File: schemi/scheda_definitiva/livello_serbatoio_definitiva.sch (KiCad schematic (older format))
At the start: 43 parts, among them J1 USB_B, J2 BTN_LED_GROUP, J3 CONN_LCD, J4 CONN_US, J5 ICSP, J6 Exp_Analog_2, J7 Exp_Analog, SW1 SW_RST, U1 FT232RL, U2 ATmega328P-PU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

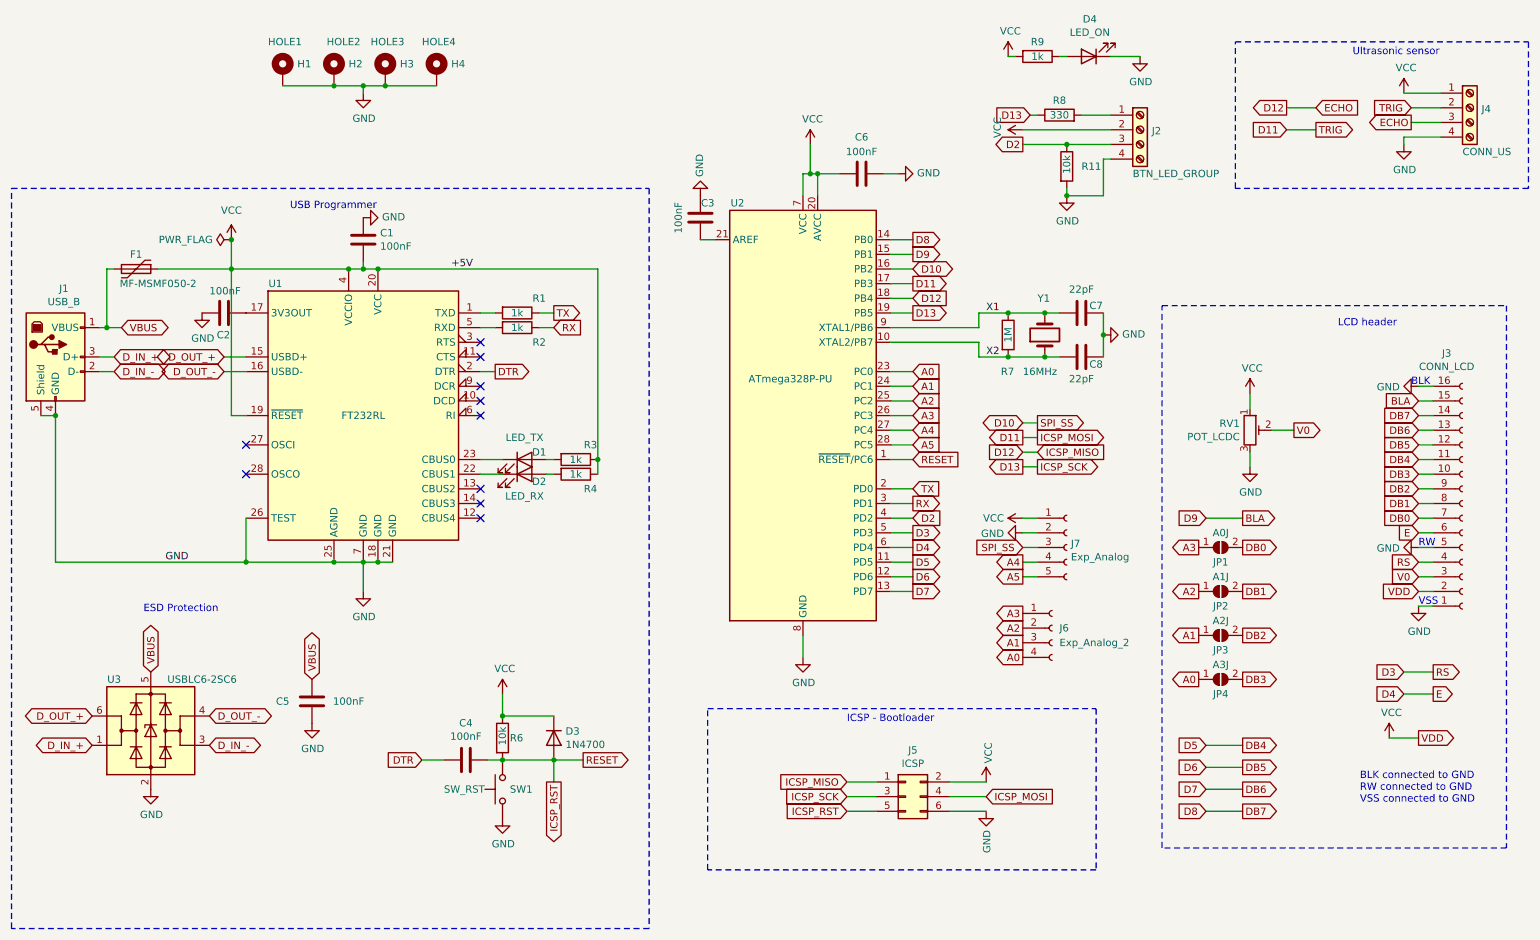
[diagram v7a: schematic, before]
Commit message: revisione pcb - fix misure lcd - spostate alcune piste
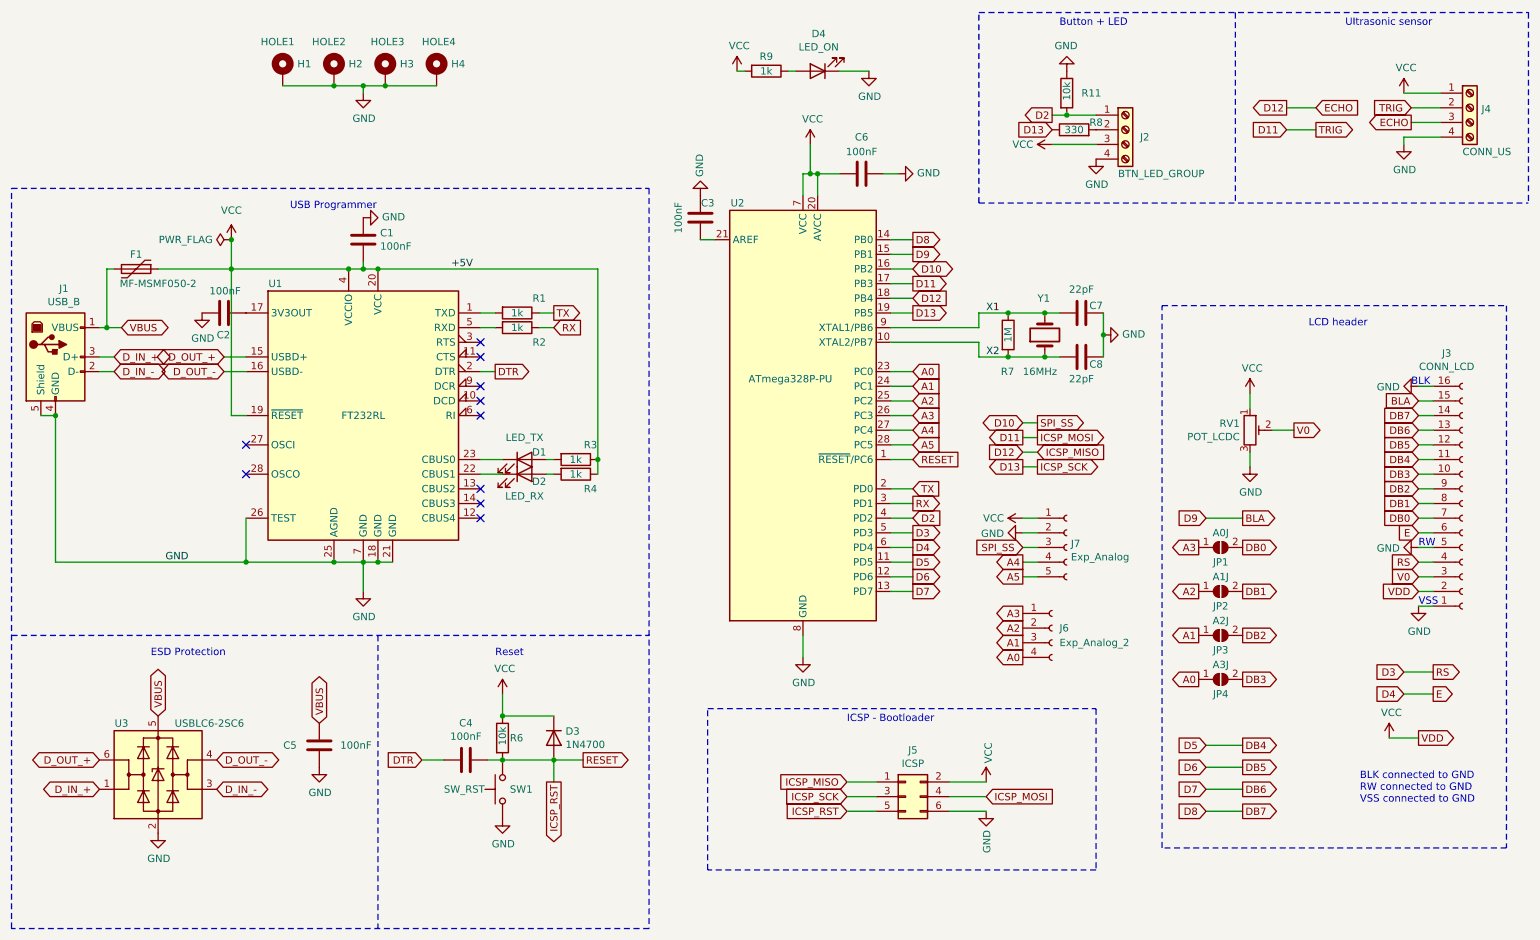
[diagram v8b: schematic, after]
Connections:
- net D2: now also J2.1 (Pin_1), R11.2; no longer J2.3 (Pin_3), R11.1
- net GND: now also R11.1; no longer R11.2
- net VCC: now also J2.3 (Pin_3); no longer J2.2 (Pin_2)
- net at R8.2: now also J2.2 (Pin_2); no longer J2.1 (Pin_1)
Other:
- note added: "Button + LED"
- note added: "Reset"
- moved on the sheet: C5, D4, J2, R11, R8, R9, U3
